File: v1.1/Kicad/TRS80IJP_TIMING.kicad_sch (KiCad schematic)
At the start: 28 parts, among them Y1 10.6445MHz

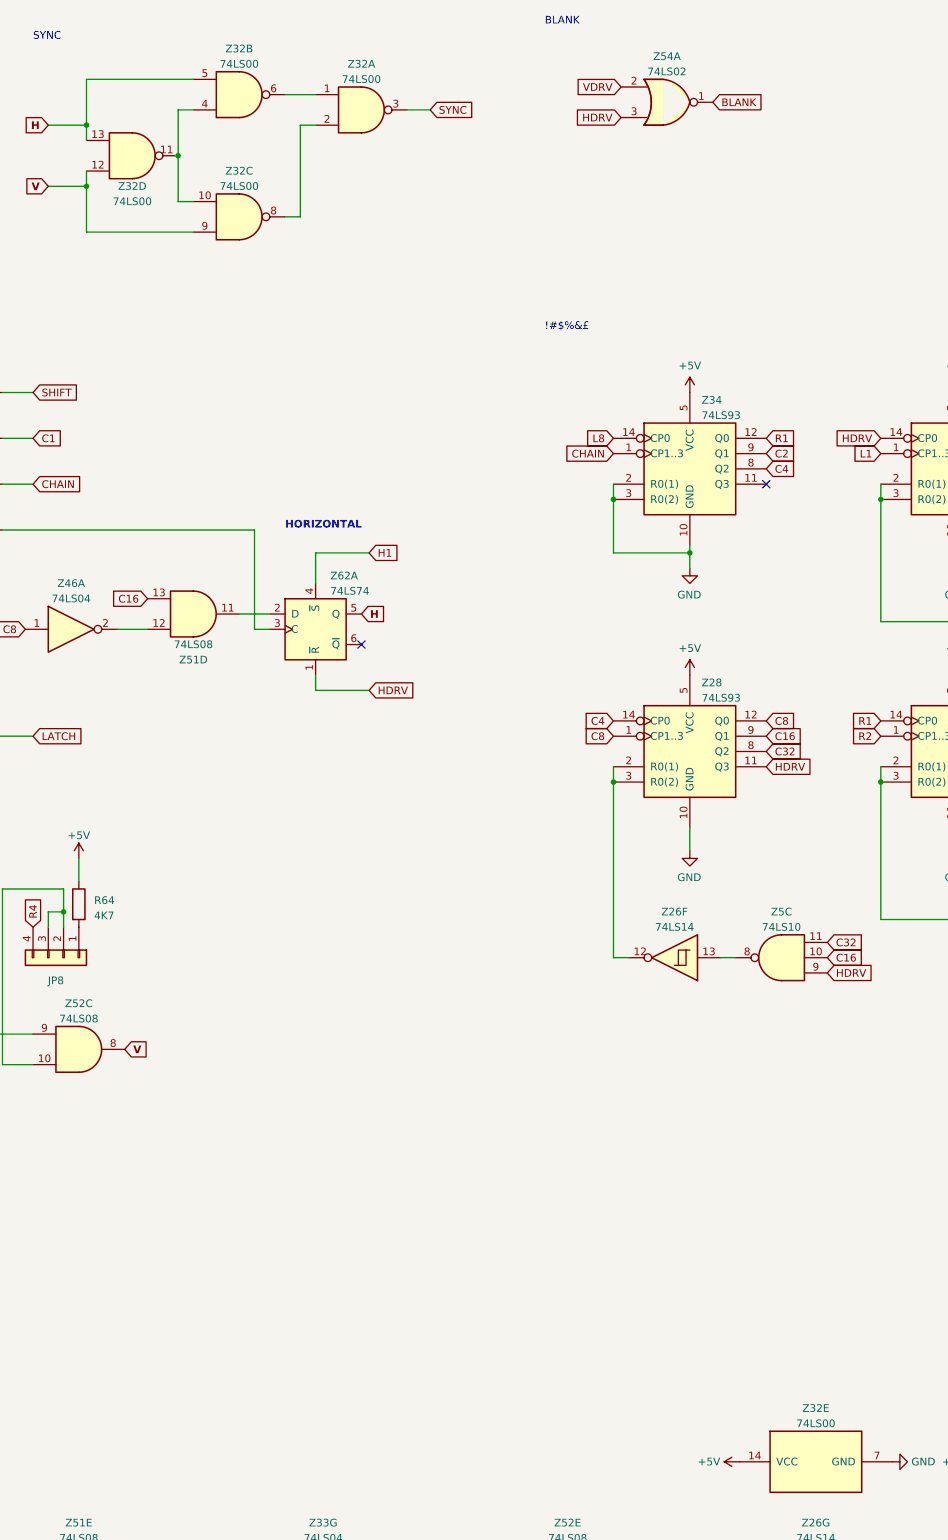
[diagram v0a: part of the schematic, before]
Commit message: Update Z32 label, Sync v1.1 Schematic to PCB
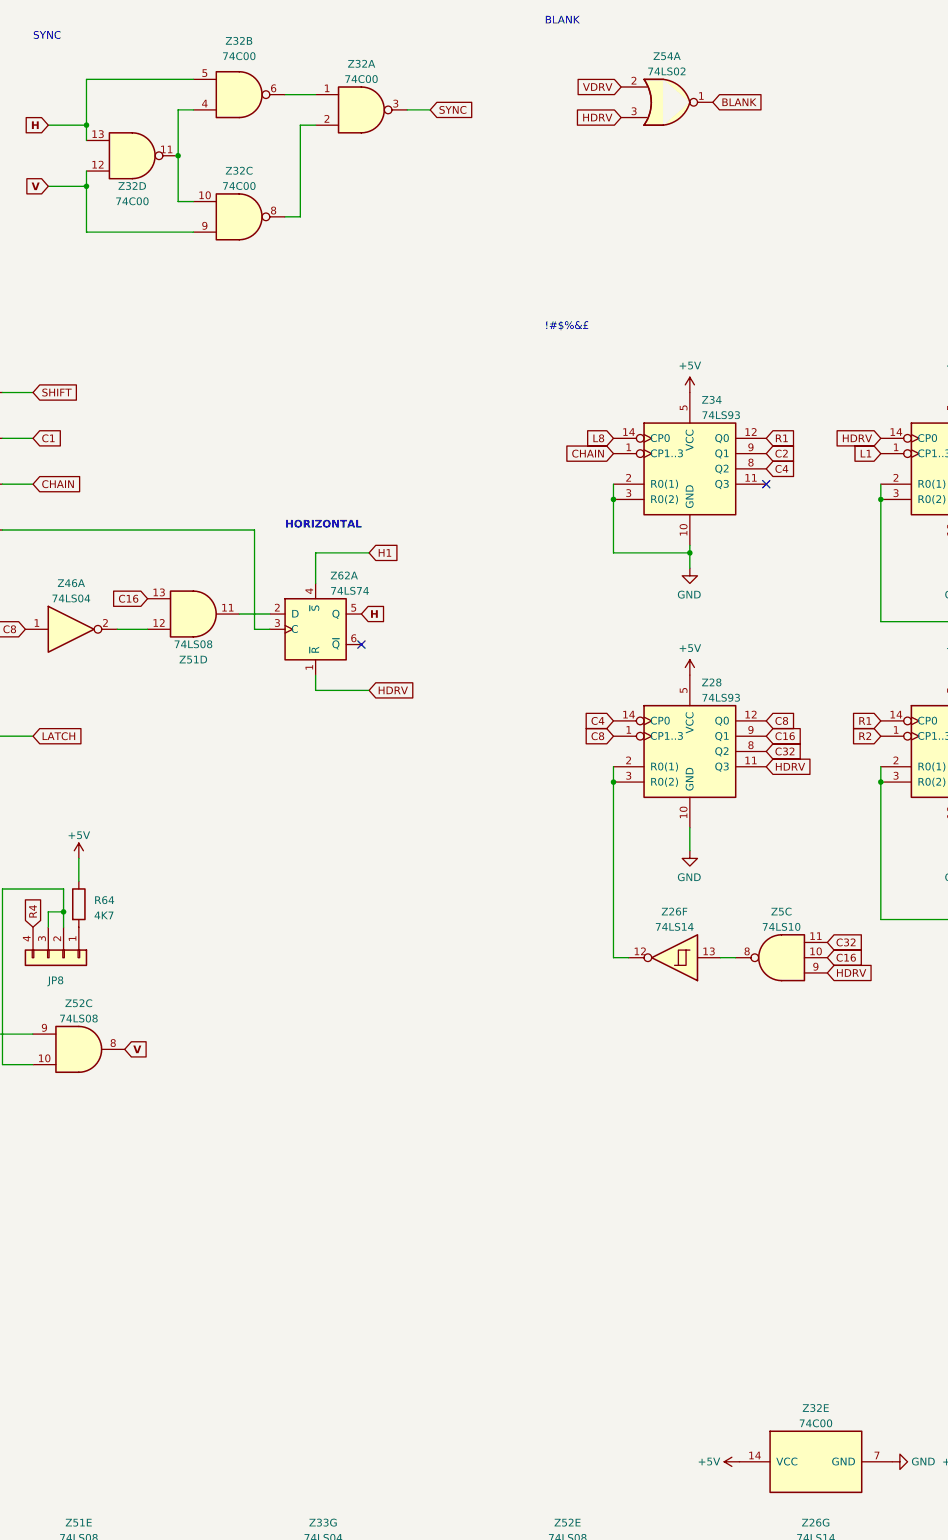
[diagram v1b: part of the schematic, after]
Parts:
- JP7: footprint TRS80:Double Wire Jumper -> TRS80:Double Wire Jumper - JP7
- Z32: value 74LS00 -> 74C00
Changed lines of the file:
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@@
   (symbol (lib_id "74xx:74LS00") (at 143.51 30.48 0) (mirror x) (unit 2)
     (in_bom yes) (on_board yes) (dnp no) (fields_autoplaced)
-    (property "Reference" "Z32" (at 143.51 22.86 0)
-      (effects (font (size 1.27 1.27)))
-    )
-    (property "Value" "74LS00" (at 143.51 25.4 0)
+    (property "Reference" "Z32" (at 143.5017 21.59 0)
+      (effects (font (size 1.27 1.27)))
+    )
+    (property "Value" "74C00" (at 143.5017 24.13 0)
       (effects (font (size 1.27 1.27)))
     )
@@
       (effects (font (size 1.27 1.27)))
     )
-    (property "Value" "74LS00" (at 143.51 45.72 0)
+    (property "Value" "74C00" (at 143.51 45.72 0)
       (effects (font (size 1.27 1.27)))
     )
@@
       (effects (font (size 1.27 1.27)))
     )
-    (property "Value" "74LS00" (at 163.83 27.94 0)
+    (property "Value" "74C00" (at 163.83 27.94 0)
       (effects (font (size 1.27 1.27)))
     )
@@
       (effects (font (size 1.27 1.27)))
     )
-    (property "Value" "74LS00" (at 125.73 48.26 0)
+    (property "Value" "74C00" (at 125.73 48.26 0)
       (effects (font (size 1.27 1.27)))
     )
@@
       (effects (font (size 1.27 1.27)) (justify left) hide)
     )
-    (property "Footprint" "TRS80:Double Wire Jumper" (at 59.69 190.5 0)
+    (property "Footprint" "TRS80:Double Wire Jumper - JP7" (at 59.69 190.5 0)
       (effects (font (size 1.27 1.27)) hide)
     )
@@
       (effects (font (size 1.27 1.27)))
     )
-    (property "Value" "74LS00" (at 239.395 251.46 90)
-      (effects (font (size 1.27 1.27)))
-    )
+    (property "Value" "74C00" (at 239.395 251.46 90)
+      (effects (font (size 1.27 1.27)))
+    )
